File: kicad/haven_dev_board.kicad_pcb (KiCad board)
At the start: 6 copper layers, 72.9 x 160.9 mm, 89 parts, among them CN1 BM46B-12DS-0.35V(51).1, J1 CLE-107-01-G-DV.1, Q1 CSD23382F4.1, Q2 CSD13380F3T.1, Q3 CSD13380F3T.1, SW1 TS2819A 230GF.1, U1 BMX160.1, U10 SN74AXC4T774RSVR.1, U12 GT-USB-9047A.1, U13 SPH0641LU4H-1.1, U14 MX25R6435FBFIL0.1, U15 ADAU1860BCBZRL.1, U2 BQ25120AYFPR.1, U3 AP22916BCA4-7.1, U4 XL-0201SURC.1, U5 KTD2026.1, U6 BQ27220YZFR.1, U8 1MΩ.1, U9 AP22916BCA4-7.1, X1 Q13FC1350000200.1

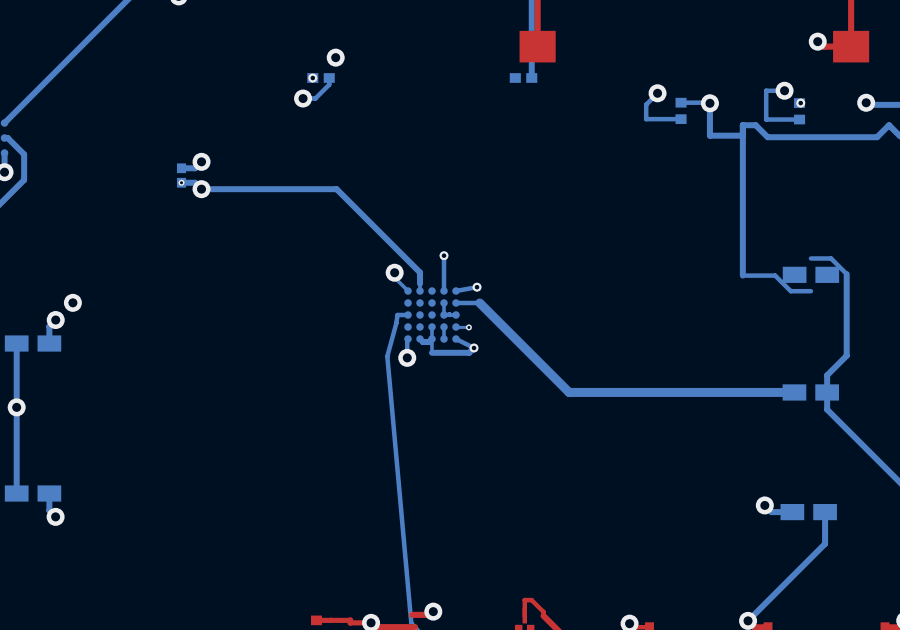
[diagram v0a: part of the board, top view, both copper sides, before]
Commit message: Bridge V_PMID's B.Cu stub to its In3.Cu plane track (45 unconnected)
Two existing fragments of the same net needed joining, not a pad
connection -- a via + short In3.Cu segment from the dangling B.Cu stub
down onto the existing long In3.Cu plane run. Verified both the via
placement and the connecting segment before placing.

DRC: 284 violations (unchanged), 46->45 unconnected, 0 new violations.

Co-Authored-By: Claude Sonnet 5 <noreply@anthropic.com>
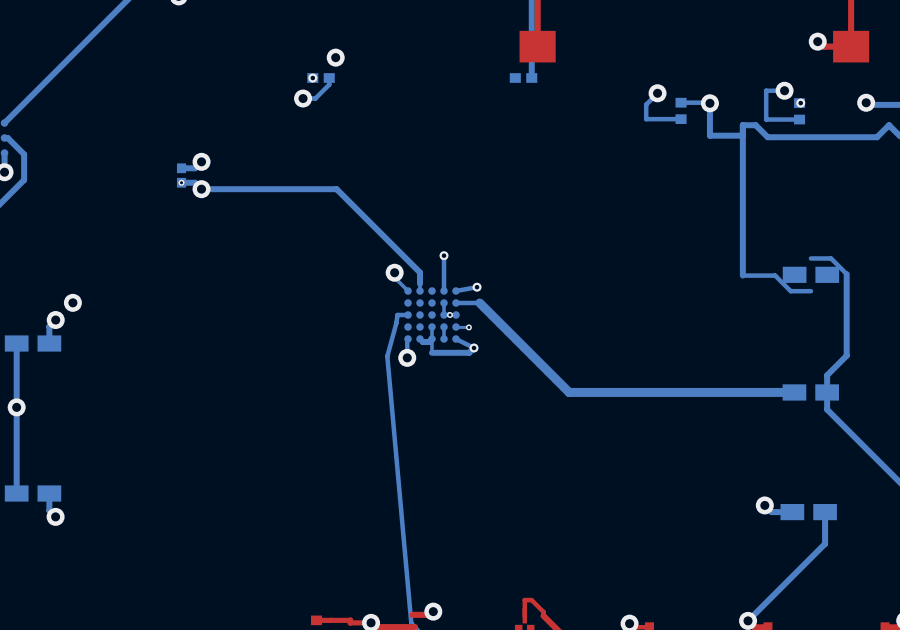
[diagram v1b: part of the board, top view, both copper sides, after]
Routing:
- net V_PMID: track 31.8 -> 32.2 mm, vias 3 -> 4
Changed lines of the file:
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@@
+	)
+	(via
+		(at 67.109 32.8772)
+		(size 0.2)
+		(drill 0.1)
+		(layers "F.Cu" "B.Cu")
+		(net 79)
 	)
 	(via
@@
 		(net 79)
 	)
+	(segment
+		(start 67.109 32.8772)
+		(end 67.109 32.472)
+		(width 0.09)
+		(layer "In3.Cu")
+		(net 79)
+	)

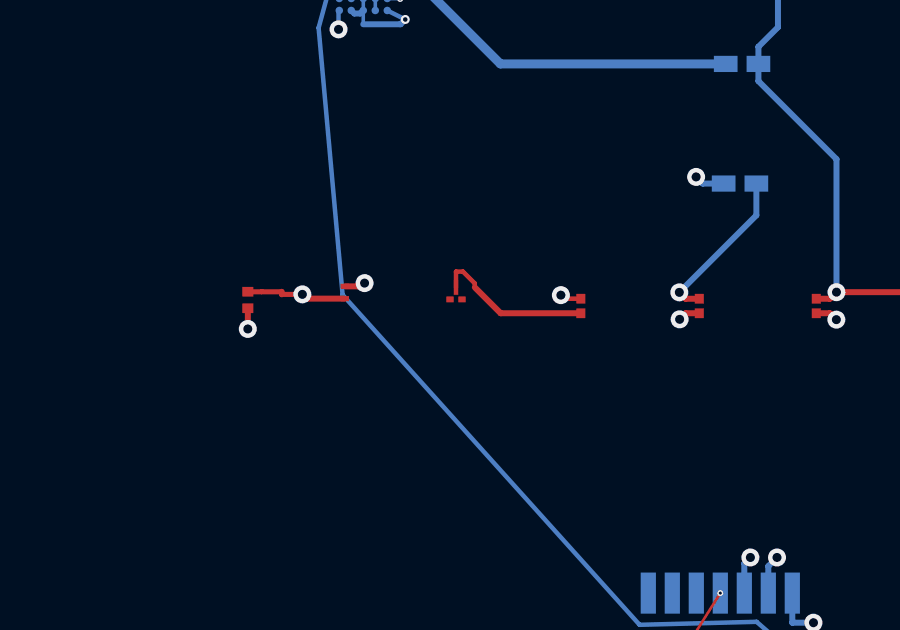
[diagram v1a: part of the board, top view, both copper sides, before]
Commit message: Connect GND to Q2 pin 2 (44 unconnected, was 45)
Q2.2 (GND) was fully enclosed by Q2's own pin 3 ($1N117) at standard
0.20mm clearance in every direction, but opens to a real 1.5mm-deep
escape at 0.15mm. Since GND is a pervasive net, a blanket exception
would loosen clearance everywhere GND runs near anything else on the
board -- scoped the .kicad_dru rule to the exact pair instead
(GND vs $1N117 only), so it can't affect GND's clearance anywhere
else. Straight via + short F.Cu jog from the existing In1.Cu stub.

DRC shows one violation relabeled (same Q2 pin-2/pin-3 pad-to-pad gap
that already existed, now reported under the new named rule instead
of the generic Default netclass rule since it's more specific) --
confirmed same UUIDs, same actual distance, not a new problem.

DRC: 284 violations (unchanged), 45->44 unconnected, 0 net-new violations.

Co-Authored-By: Claude Sonnet 5 <noreply@anthropic.com>
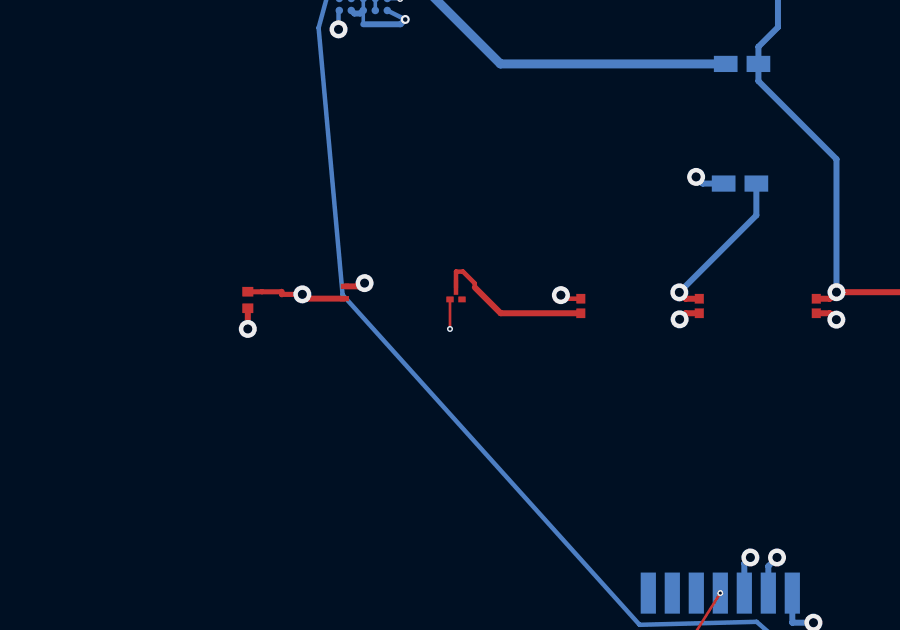
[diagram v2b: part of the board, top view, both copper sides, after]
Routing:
- net GND: track 662.8 -> 663.8 mm, vias 54 -> 55
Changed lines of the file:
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@@
+	)
+	(segment
+		(start 69.3998 44.2929)
+		(end 69.3998 43.3077)
+		(width 0.09)
+		(layer "F.Cu")
+		(net 25)
 	)
 	(segment
@@
 		(layers "F.Cu" "B.Cu")
 		(net 25)
+	)
+	(via
+		(at 69.3998 44.2929)
+		(size 0.2)
+		(drill 0.1)
+		(layers "F.Cu" "B.Cu")
+		(net 25)

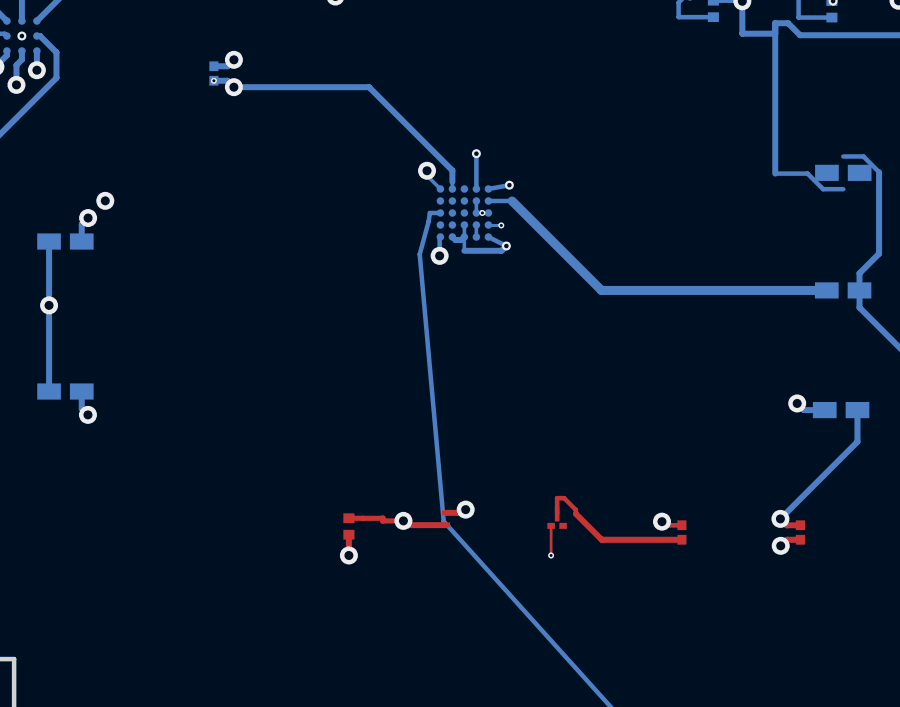
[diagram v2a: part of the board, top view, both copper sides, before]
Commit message: Connect 3V3 to U2.C5 (43 unconnected, was 44)
Real escape lane confirmed at standard 0.20mm clearance -- multi-layer
pathfinder found the F.Cu run instantly, but its endpoint landed on
U2.C5's XY coordinate on the wrong layer (F.Cu, empty board there --
the real pad is B.Cu only), same class of miss as earlier sessions.
Fixed with a via + short B.Cu jog to the actual pad.

DRC: 284 violations (unchanged), 44->43 unconnected, 0 new violations.

Co-Authored-By: Claude Sonnet 5 <noreply@anthropic.com>
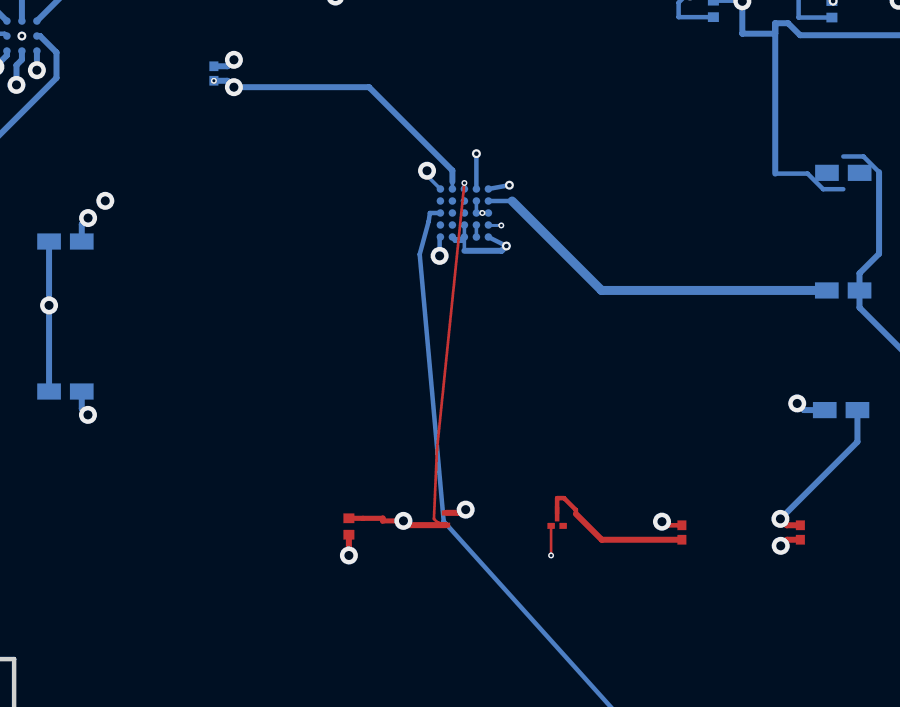
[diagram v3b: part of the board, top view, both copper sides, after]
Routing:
- net 3V3: track 187.3 -> 199.2 mm, vias 7 -> 8
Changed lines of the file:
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@@
+	)
+	(segment
+		(start 65.8949 43.2827)
+		(end 65.5949 43.1771)
+		(width 0.09)
+		(layer "F.Cu")
+		(net 15)
+	)
+	(segment
+		(start 65.5949 43.1771)
+		(end 65.4949 43.0771)
+		(width 0.09)
+		(layer "F.Cu")
+		(net 15)
 	)
 	(segment
@@
 	)
 	(segment
+		(start 65.5949 40.7771)
+		(end 66.5098 31.8771)
+		(width 0.09)
+		(layer "F.Cu")
+		(net 15)
+	)
+	(segment
 		(start 111.1598 31.4861)
 		(end 111.1598 34.2036)
@@
 	)
 	(segment
+		(start 65.4949 43.0771)
+		(end 65.5949 40.7771)
+		(width 0.09)
+		(layer "F.Cu")
+		(net 15)
+	)
+	(segment
 		(start 62.6603 43.0534)
 		(end 63.1311 43.0534)
@@
 	)
 	(via
+		(at 66.5098 31.8771)
+		(size 0.2)
+		(drill 0.1)
+		(layers "F.Cu" "B.Cu")
+		(net 15)
+	)
+	(via
 		(at 110.9304 31.2567)
 		(size 0.6)
@@
 		(layer "B.Cu")
 		(net 15)
+	)
+	(segment
+		(start 66.5098 31.8771)
+		(end 66.5098 32.0771)
+		(width 0.09)
+		(layer "B.Cu")
+		(net 15)

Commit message: Connect V_LS via to U14.D2 (42 unconnected, was 43)
Real escape lane on B.Cu at standard 0.20mm clearance -- D2 is F.Cu
only, so added the via + short F.Cu jog rather than trusting the
B.Cu pathfind's "ok" result at D2's XY (same wrong-layer class of
issue as before, checked for explicitly this time).

U14.H4<->D2 (both V_LS, adjacent U14 pads) and the two U10-area B.Cu
V_LS stubs remain unconnected -- H4's only real escape direction
points away from D2, and the U10 stubs sit on the far side of the
same tightly-packed SPI bus wall that's blocked several other nets
this session. U15's three internal V_LS pairs (A2/B5, F3/G2, F3/F7)
are confirmed unroutable -- pad center itself blocked at standard
clearance, same fully-interior-BGA-ball class as the GND/$1N151
pads found earlier.

DRC: 283 violations (unchanged), 43->42 unconnected, 0 new violations.

Co-Authored-By: Claude Sonnet 5 <noreply@anthropic.com>
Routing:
- net V_LS: track 285.9 -> 295.3 mm, vias 21 -> 22
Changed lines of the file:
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@@
+	)
+	(segment
+		(start 104.8598 110.800805)
+		(end 104.7598 110.6276)
+		(width 0.09)
+		(layer "F.Cu")
+		(net 78)
 	)
 	(segment
@@
 	)
 	(via
+		(at 104.8598 110.800805)
+		(size 0.2)
+		(drill 0.1)
+		(layers "F.Cu" "B.Cu")
+		(net 78)
+	)
+	(via
 		(at 48.5563 110.5491)
 		(size 0.6)
@@
 		(layer "B.Cu")
 		(net 78)
+	)
+	(segment
+		(start 97.8598 116.8499)
+		(end 104.8598 110.800805)
+		(width 0.09)
+		(layer "B.Cu")
+		(net 78)

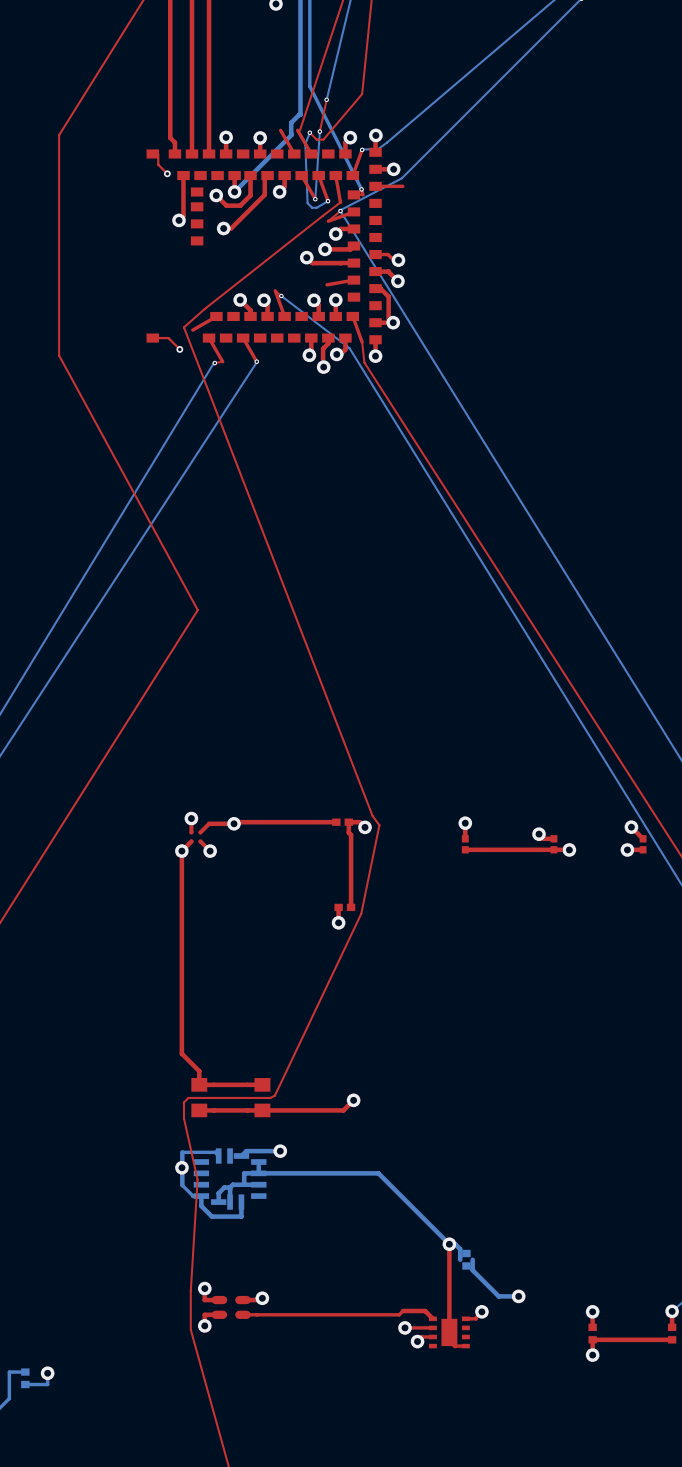
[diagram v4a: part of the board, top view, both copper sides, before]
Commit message: Route SCL, MDBT531 to U5 (41 unconnected, was 42)
A 17th MDBT531 signal never in the original tracked list -- SCL and
SDA both connect MDBT531 directly to U5, discovered only by scanning
the DRC unconnected-items list broadly rather than trusting the
session's earlier net list. Extensive existing routing already
existed between the MDBT531 stub and other points (from earlier
Codex/Luna work), but never actually reached U5 -- confirmed via real
pathfinding, not assumed from the copper's presence.

Real escape lanes on both ends at standard 0.20mm clearance; the long
(~52mm) run needed the multi-layer pathfinder (single-layer attempts
on both F.Cu and B.Cu exhausted without a path).

Two real mistakes caught before landing:
1. The multi-layer pathfinder landed BOTH endpoints on the wrong layer
   (empty board space at each pad's XY, not the real copper) -- fixed
   with vias + jogs at each end, verified against the real pad layers
   this time rather than trusting the "ok" status.
2. Forgot the two INTERNAL layer-transition vias where the path
   crosses between F.Cu and B.Cu partway through -- matching endpoint
   coordinates across different layers looks connected but isn't
   without an actual via there. Caught via the unconnected-items list
   (not the violation count, which looked fine) showing two segments
   ending at the same XY on different layers, still listed as not
   joined. Also discovered a duplicate via had been placed exactly on
   top of a pre-existing one from earlier work -- removed the
   duplicate and reused the existing via instead of shipping a
   "holes_co_located" warning.

DRC: 282 violations (unchanged), 42->41 unconnected, 0 new violations.

Co-Authored-By: Claude Sonnet 5 <noreply@anthropic.com>
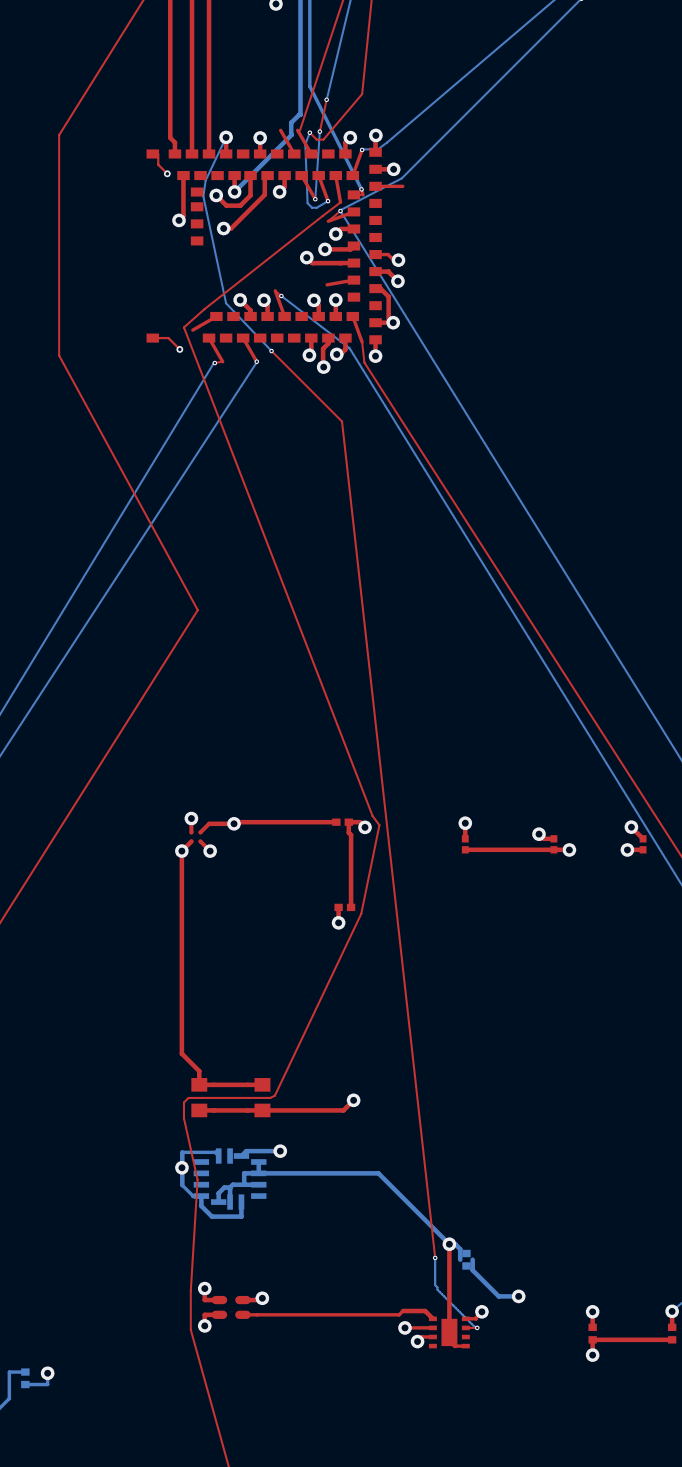
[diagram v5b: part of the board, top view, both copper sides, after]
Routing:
- net SCL: track 64.0 -> 120.3 mm, vias 4 -> 7

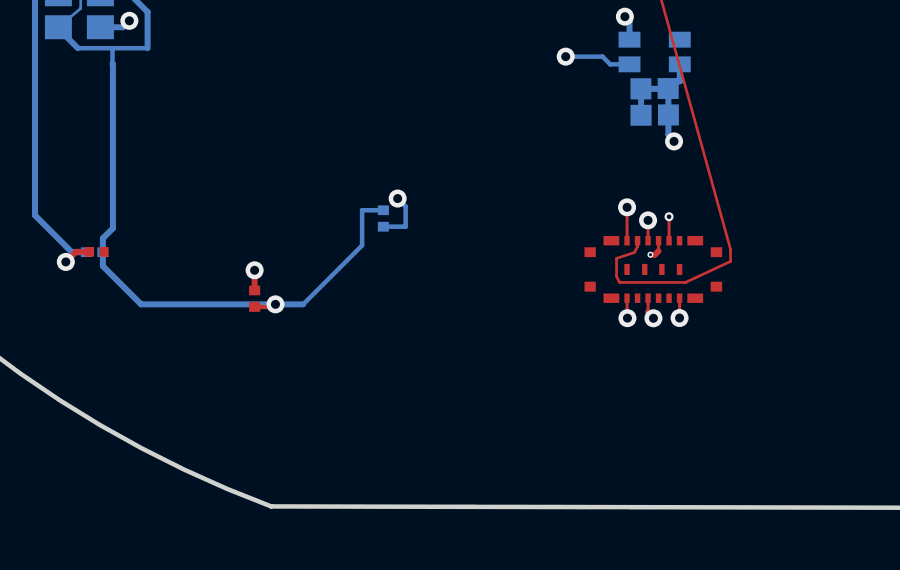
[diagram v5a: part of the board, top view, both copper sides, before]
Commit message: Close 3V3 end to end: CN1.3 branch routed (40 unconnected, was 41)
Added the second exception this needed (3V3 vs SDA2, 0.10mm -- an
existing SDA2 via sits 0.1022mm from the route's path, confirmed
already, independently correct regardless of the route's fate) on
top of the existing PDMCLK one. Both together still didn't let
astar_mixed find a full path from the far stub straight through to
the CN1.3 pad -- traced it to the same early-exit imprecision
documented for SCL: the only real escape angle (80 degrees) is a
single narrow lane, and pathfinding to the raw pad target kept
missing it. Fixed the same way as SCL: pathfind to the confirmed
escape point instead of the pad, verify a real connecting segment
from the pathfinder's raw last point to that escape point, then a
final verified segment from there to the pad itself.

DRC: 281 violations (unchanged), 41->40 unconnected, 0 new violations.

Co-Authored-By: Claude Sonnet 5 <noreply@anthropic.com>
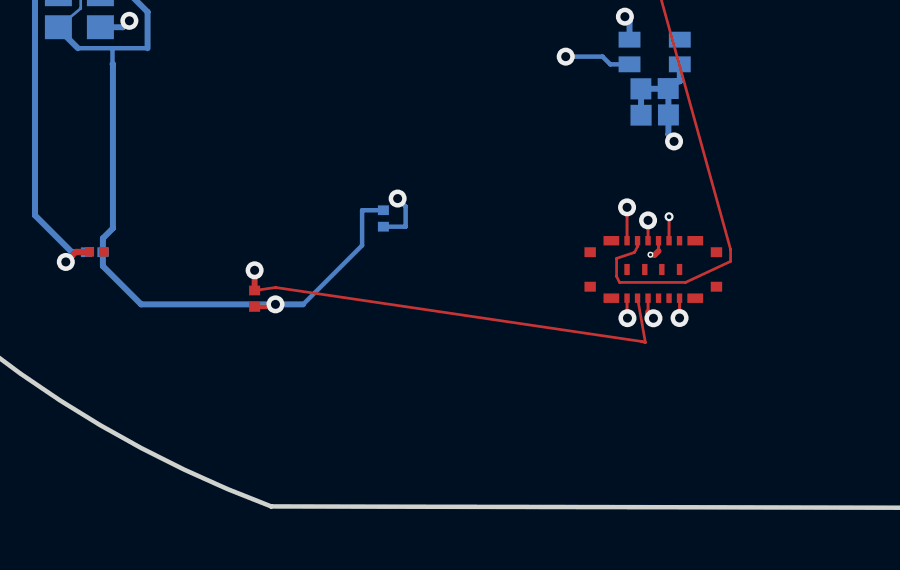
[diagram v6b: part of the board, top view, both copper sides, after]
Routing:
- net 3V3: track 199.2 -> 213.9 mm
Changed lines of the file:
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@@
+	)
+	(segment
+		(start 78.142372 136.262411)
+		(end 77.8819 134.7852)
+		(width 0.09)
+		(layer "F.Cu")
+		(net 15)
 	)
 	(segment
@@
 	)
 	(segment
+		(start 65.8173 134.4284)
+		(end 78.0173 136.2284)
+		(width 0.09)
+		(layer "F.Cu")
+		(net 15)
+	)
+	(segment
 		(start 94.3623 117.553)
 		(end 94.3623 117.5531)
@@
 	)
 	(segment
+		(start 65.1173 134.5284)
+		(end 65.8173 134.4284)
+		(width 0.09)
+		(layer "F.Cu")
+		(net 15)
+	)
+	(segment
 		(start 111.1598 34.2036)
 		(end 111.16 34.2036)
@@
 		(layer "F.Cu")
 		(net 15)
+	)
+	(segment
+		(start 78.0173 136.2284)
+		(end 78.142372 136.262411)
+		(width 0.09)
+		(layer "F.Cu")
+		(net 15)
